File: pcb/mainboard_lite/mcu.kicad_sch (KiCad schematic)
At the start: 29 parts, among them J1 USB_C_Receptacle_USB2.0, J5 SM03B-SRSS-TB, SW401 SW_Push, SW701 TS-1007S-AR02516, U14 RP2040, U603 USBLC6-2P6, U701 W25Q32JV, Y701 12MHz

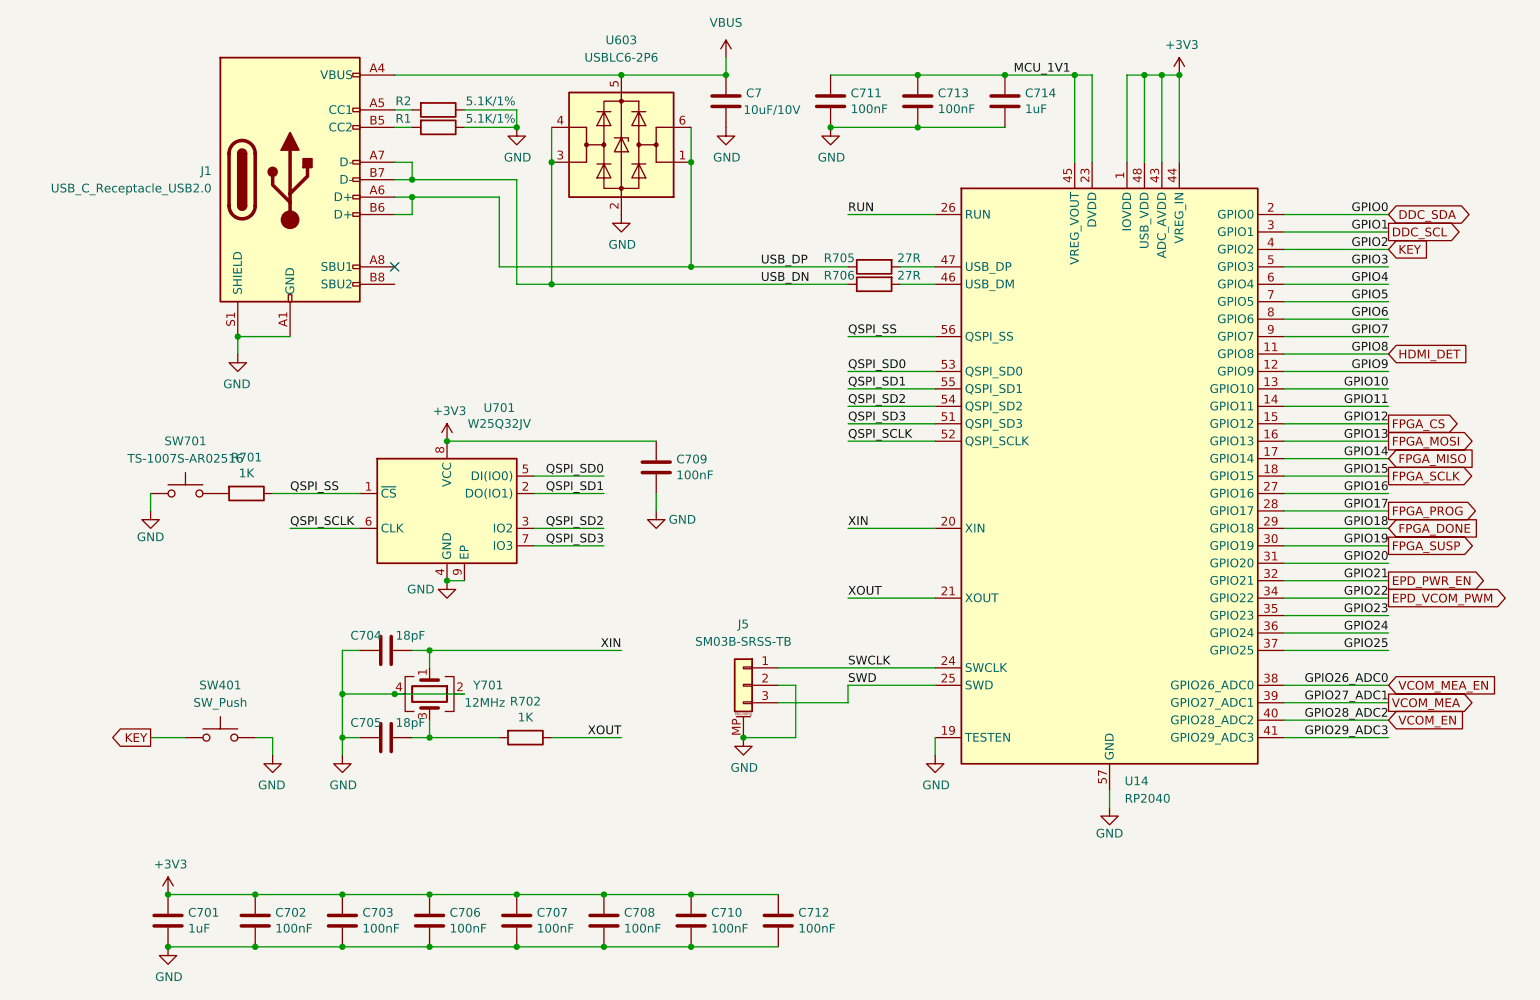
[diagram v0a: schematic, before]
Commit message: lite r0p1 schematic fixes
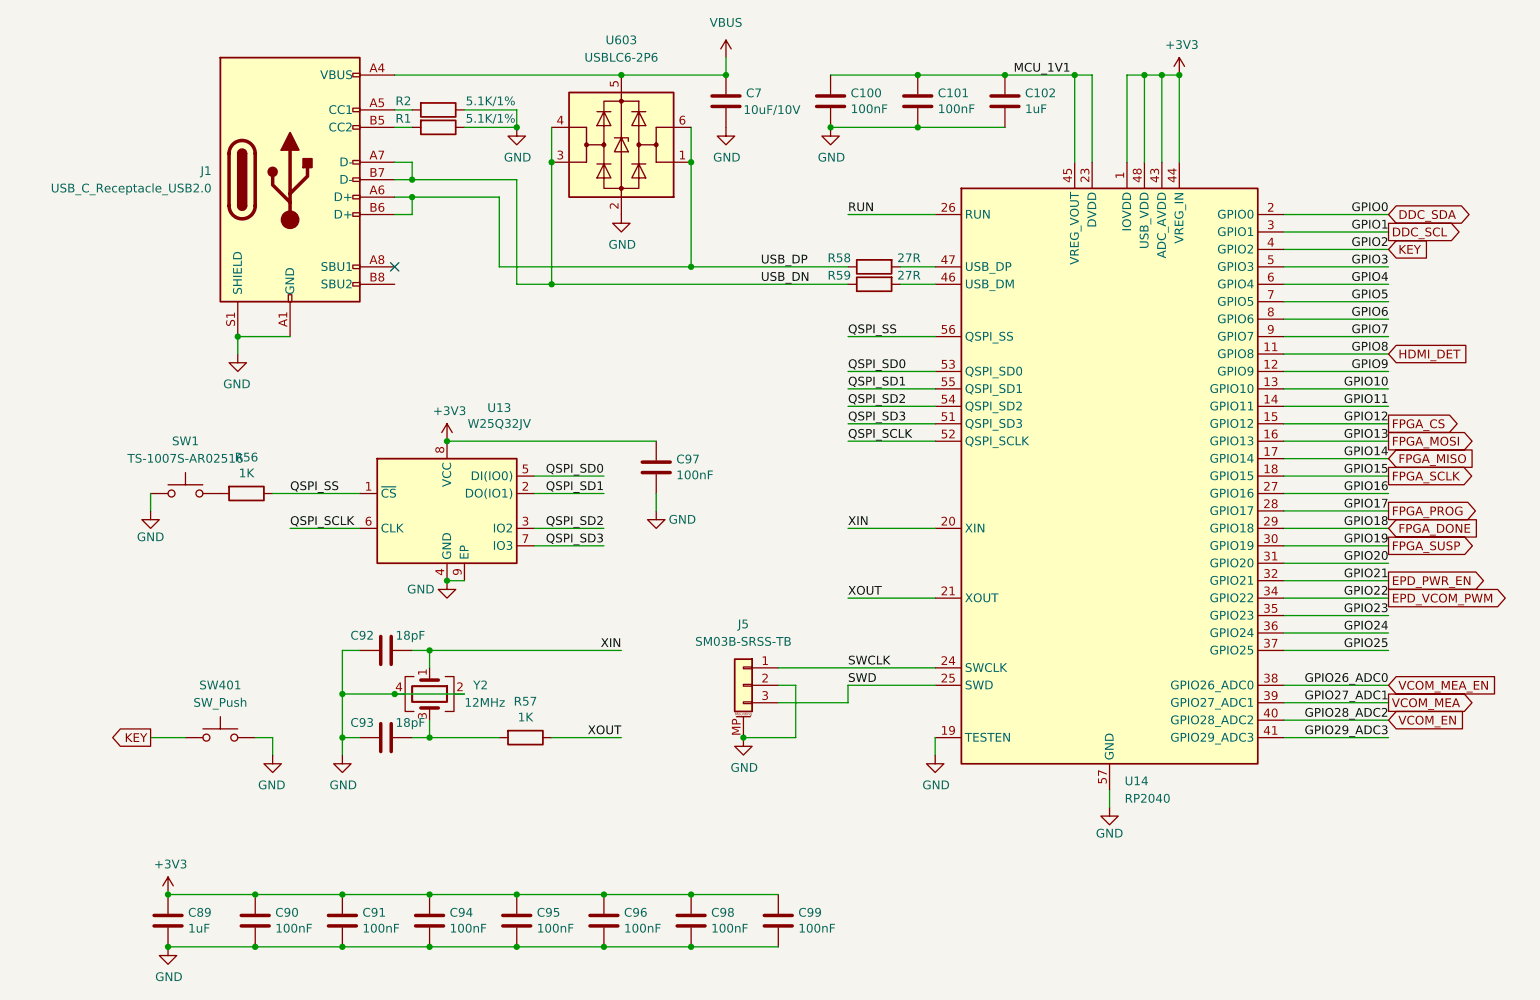
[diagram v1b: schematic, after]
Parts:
- renumbered C711 to C100, C713 to C101, C714 to C102, C701 to C89, C702 to C90, C703 to C91, C704 to C92, C705 to C93, C706 to C94, C707 to C95, C708 to C96, C709 to C97, C710 to C98, C712 to C99, R701 to R56, R702 to R57, R705 to R58, R706 to R59, SW701 to SW1, U701 to U13, Y701 to Y2
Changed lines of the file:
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@@
   (symbol (lib_id "Device:C") (at 81.28 166.37 0) (unit 1)
     (in_bom yes) (on_board yes) (dnp no)
-    (property "Reference" "C703" (at 84.201 165.2016 0)
+    (property "Reference" "C91" (at 84.201 165.2016 0)
       (effects (font (size 1.27 1.27)) (justify left))
     )
@@
   (symbol (lib_id "power:GND") (at 152.4 50.8 0) (unit 1)
     (in_bom yes) (on_board yes) (dnp no)
-    (property "Reference" "#PWR0158" (at 152.4 57.15 0)
+    (property "Reference" "#PWR0137" (at 152.4 57.15 0)
       (effects (font (size 1.27 1.27)) hide)
     )
@@
   (symbol (lib_id "Switch:SW_Push") (at 58.42 104.14 0) (mirror y) (unit 1)
     (in_bom yes) (on_board yes) (dnp no)
-    (property "Reference" "SW701" (at 58.42 96.52 0)
+    (property "Reference" "SW1" (at 58.42 96.52 0)
       (effects (font (size 1.27 1.27)))
     )
@@
   (symbol (lib_id "power:GND") (at 167.64 142.24 0) (unit 1)
     (in_bom yes) (on_board yes) (dnp no)
-    (property "Reference" "#PWR0161" (at 167.64 148.59 0)
+    (property "Reference" "#PWR0138" (at 167.64 148.59 0)
       (effects (font (size 1.27 1.27)) hide)
     )
@@
   (symbol (lib_id "Device:R") (at 107.95 139.7 270) (unit 1)
     (in_bom yes) (on_board yes) (dnp no)
-    (property "Reference" "R702" (at 107.95 134.4422 90)
+    (property "Reference" "R57" (at 107.95 134.4422 90)
       (effects (font (size 1.27 1.27)))
     )
@@
   (symbol (lib_id "power:+3V3") (at 203.2 43.18 0) (unit 1)
     (in_bom yes) (on_board yes) (dnp no)
-    (property "Reference" "#PWR0171" (at 203.2 46.99 0)
+    (property "Reference" "#PWR0140" (at 203.2 46.99 0)
       (effects (font (size 1.27 1.27)) hide)
     )
@@
   (symbol (lib_id "Device:C") (at 93.98 166.37 0) (unit 1)
     (in_bom yes) (on_board yes) (dnp no)
-    (property "Reference" "C706" (at 96.901 165.2016 0)
+    (property "Reference" "C94" (at 96.901 165.2016 0)
       (effects (font (size 1.27 1.27)) (justify left))
     )
@@
   (symbol (lib_id "power:GND") (at 81.28 142.24 0) (unit 1)
     (in_bom yes) (on_board yes) (dnp no)
-    (property "Reference" "#PWR0165" (at 81.28 148.59 0)
+    (property "Reference" "#PWR0133" (at 81.28 148.59 0)
       (effects (font (size 1.27 1.27)) hide)
     )
@@
   (symbol (lib_id "Device:C") (at 119.38 166.37 0) (unit 1)
     (in_bom yes) (on_board yes) (dnp no)
-    (property "Reference" "C708" (at 122.301 165.2016 0)
+    (property "Reference" "C96" (at 122.301 165.2016 0)
       (effects (font (size 1.27 1.27)) (justify left))
     )
@@
   (symbol (lib_id "Device:C") (at 68.58 166.37 0) (unit 1)
     (in_bom yes) (on_board yes) (dnp no)
-    (property "Reference" "C702" (at 71.501 165.2016 0)
+    (property "Reference" "C90" (at 71.501 165.2016 0)
       (effects (font (size 1.27 1.27)) (justify left))
     )
@@
   (symbol (lib_id "Device:C") (at 55.88 166.37 0) (unit 1)
     (in_bom yes) (on_board yes) (dnp no)
-    (property "Reference" "C701" (at 58.801 165.202 0)
+    (property "Reference" "C89" (at 58.801 165.202 0)
       (effects (font (size 1.27 1.27)) (justify left))
     )
@@
   (symbol (lib_id "power:GND") (at 193.04 149.86 0) (unit 1)
     (in_bom yes) (on_board yes) (dnp no)
-    (property "Reference" "#PWR0160" (at 193.04 156.21 0)
+    (property "Reference" "#PWR0139" (at 193.04 156.21 0)
       (effects (font (size 1.27 1.27)) hide)
     )
@@
   (symbol (lib_id "Device:C") (at 165.1 46.99 0) (unit 1)
     (in_bom yes) (on_board yes) (dnp no)
-    (property "Reference" "C713" (at 168.021 45.8216 0)
+    (property "Reference" "C101" (at 168.021 45.8216 0)
       (effects (font (size 1.27 1.27)) (justify left))
     )
@@
   (symbol (lib_id "Device:C") (at 127 100.33 0) (unit 1)
     (in_bom yes) (on_board yes) (dnp no)
-    (property "Reference" "C709" (at 129.921 99.1616 0)
+    (property "Reference" "C97" (at 129.921 99.1616 0)
       (effects (font (size 1.27 1.27)) (justify left))
     )
@@
   (symbol (lib_id "power:GND") (at 53.34 106.68 0) (unit 1)
     (in_bom yes) (on_board yes) (dnp no)
-    (property "Reference" "#PWR0164" (at 53.34 113.03 0)
+    (property "Reference" "#PWR0129" (at 53.34 113.03 0)
       (effects (font (size 1.27 1.27)) hide)
     )
@@
   (symbol (lib_id "Device:R") (at 158.75 73.66 90) (mirror x) (unit 1)
     (in_bom yes) (on_board yes) (dnp no)
-    (property "Reference" "R706" (at 153.67 72.39 90)
+    (property "Reference" "R59" (at 153.67 72.39 90)
       (effects (font (size 1.27 1.27)))
     )
@@
   (symbol (lib_id "Device:C") (at 132.08 166.37 0) (unit 1)
     (in_bom yes) (on_board yes) (dnp no)
-    (property "Reference" "C710" (at 135.001 165.2016 0)
+    (property "Reference" "C98" (at 135.001 165.2016 0)
       (effects (font (size 1.27 1.27)) (justify left))
     )
@@
   (symbol (lib_id "power:+3V3") (at 55.88 162.56 0) (unit 1)
     (in_bom yes) (on_board yes) (dnp no)
-    (property "Reference" "#PWR0162" (at 55.88 166.37 0)
+    (property "Reference" "#PWR0130" (at 55.88 166.37 0)
       (effects (font (size 1.27 1.27)) hide)
     )
@@
   (symbol (lib_id "Device:C") (at 106.68 166.37 0) (unit 1)
     (in_bom yes) (on_board yes) (dnp no)
-    (property "Reference" "C707" (at 109.601 165.2016 0)
+    (property "Reference" "C95" (at 109.601 165.2016 0)
       (effects (font (size 1.27 1.27)) (justify left))
     )
@@
   (symbol (lib_id "Device:C") (at 87.63 127 270) (unit 1)
     (in_bom yes) (on_board yes) (dnp no)
-    (property "Reference" "C704" (at 82.4484 124.841 90)
+    (property "Reference" "C92" (at 82.4484 124.841 90)
       (effects (font (size 1.27 1.27)) (justify left))
     )
@@
   (symbol (lib_id "power:GND") (at 127 106.68 0) (unit 1)
     (in_bom yes) (on_board yes) (dnp no)
-    (property "Reference" "#PWR0168" (at 127 113.03 0)
+    (property "Reference" "#PWR0136" (at 127 113.03 0)
       (effects (font (size 1.27 1.27)) hide)
     )
@@
   (symbol (lib_id "Device:R") (at 67.31 104.14 270) (unit 1)
     (in_bom yes) (on_board yes) (dnp no)
-    (property "Reference" "R701" (at 67.31 98.8822 90)
+    (property "Reference" "R56" (at 67.31 98.8822 90)
       (effects (font (size 1.27 1.27)))
     )
@@
   (symbol (lib_id "Device:C") (at 177.8 46.99 0) (unit 1)
     (in_bom yes) (on_board yes) (dnp no)
-    (property "Reference" "C714" (at 180.721 45.8216 0)
+    (property "Reference" "C102" (at 180.721 45.8216 0)
       (effects (font (size 1.27 1.27)) (justify left))
     )
@@
   (symbol (lib_id "power:GND") (at 55.88 170.18 0) (unit 1)
     (in_bom yes) (on_board yes) (dnp no)
-    (property "Reference" "#PWR0163" (at 55.88 176.53 0)
+    (property "Reference" "#PWR0131" (at 55.88 176.53 0)
       (effects (font (size 1.27 1.27)) hide)
     )
@@
   (symbol (lib_id "power:GND") (at 139.7 139.7 0) (unit 1)
     (in_bom yes) (on_board yes) (dnp no)
-    (property "Reference" "#PWR0161" (at 139.7 146.05 0)
+    (property "Reference" "#PWR0144" (at 139.7 146.05 0)
       (effects (font (size 1.27 1.27)) hide)
     )
@@
   (symbol (lib_id "Memory_Flash:W25Q32JVZP") (at 96.52 106.68 0) (unit 1)
     (in_bom yes) (on_board yes) (dnp no)
-    (property "Reference" "U701" (at 104.14 91.669 0)
+    (property "Reference" "U13" (at 104.14 91.669 0)
       (effects (font (size 1.27 1.27)))
     )
@@
   (symbol (lib_id "power:+3V3") (at 96.52 96.52 0) (unit 1)
     (in_bom yes) (on_board yes) (dnp no)
-    (property "Reference" "#PWR0166" (at 96.52 100.33 0)
+    (property "Reference" "#PWR0134" (at 96.52 100.33 0)
       (effects (font (size 1.27 1.27)) hide)
     )
@@
   (symbol (lib_id "Device:C") (at 87.63 139.7 270) (unit 1)
     (in_bom yes) (on_board yes) (dnp no)
-    (property "Reference" "C705" (at 82.4484 137.541 90)
+    (property "Reference" "C93" (at 82.4484 137.541 90)
       (effects (font (size 1.27 1.27)) (justify left))
     )
@@
   (symbol (lib_id "power:GND") (at 96.52 116.84 0) (unit 1)
     (in_bom yes) (on_board yes) (dnp no)
-    (property "Reference" "#PWR0167" (at 96.52 123.19 0)
+    (property "Reference" "#PWR0135" (at 96.52 123.19 0)
       (effects (font (size 1.27 1.27)) hide)
     )
@@
   (symbol (lib_id "Device:C") (at 152.4 46.99 0) (unit 1)
     (in_bom yes) (on_board yes) (dnp no)
-    (property "Reference" "C711" (at 155.321 45.8216 0)
+    (property "Reference" "C100" (at 155.321 45.8216 0)
       (effects (font (size 1.27 1.27)) (justify left))
     )
@@
   (symbol (lib_id "Device:C") (at 144.78 166.37 0) (unit 1)
     (in_bom yes) (on_board yes) (dnp no)
-    (property "Reference" "C712" (at 147.701 165.2016 0)
+    (property "Reference" "C99" (at 147.701 165.2016 0)
       (effects (font (size 1.27 1.27)) (justify left))
     )
@@
   (symbol (lib_id "Device:R") (at 158.75 71.12 90) (mirror x) (unit 1)
     (in_bom yes) (on_board yes) (dnp no)
-    (property "Reference" "R705" (at 153.67 69.85 90)
+    (property "Reference" "R58" (at 153.67 69.85 90)
       (effects (font (size 1.27 1.27)))
     )
@@
   (symbol (lib_id "Device:Crystal_GND24") (at 93.98 133.35 270) (unit 1)
     (in_bom yes) (on_board yes) (dnp no)
-    (property "Reference" "Y701" (at 100.33 132.08 90)
-      (effects (font (size 1.27 1.27)) (justify left))
-    )
+    (property "Reference" "Y2" (at 100.33 132.08 90)
+      (effects (font (size 1.27 1.27)) (justify left))
+    )
